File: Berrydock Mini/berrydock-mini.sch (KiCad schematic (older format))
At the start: 94 parts, among them J1 RJ45, P1 CONN_01X16, P2 CONN_01X11, P3 CONN_01X04, P4 CONN_01X03, P5 USB_OTG, P6 USB_A, SW1 SWITCH_INV, SW2 BUTTON, U1 USBLC6-2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

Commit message: laid everything out
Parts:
- removed C2, C3: 100nF, Capacitors_SMD:C_0603, symbol C_Small
- removed JP1, JP2: Jumper_NO_Small, Pin_Headers:Pin_Header_Straight_1x02, symbol Jumper_NO_Small
- removed R2: 2K, Resistors_SMD:R_0603_HandSoldering, symbol R_Small
- removed R3: 3K, Resistors_SMD:R_0603_HandSoldering, symbol R_Small
- removed U1, U2: USBLC6-2, Omega2-Berrydock:SOT32-6L, symbol USBLC6-2
- removed U6, U7: SMP75, Omega2-Berrydock:DO-214AA, symbol SMP75
- R11, R12, R6, R7, R8, R9: footprint Resistors_SMD:R_0603_HandSoldering -> Resistors_SMD:R_0603
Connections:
- net labels removed: CHARGE
- wire segments 368 -> 326
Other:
- note removed: "Power Sensing"

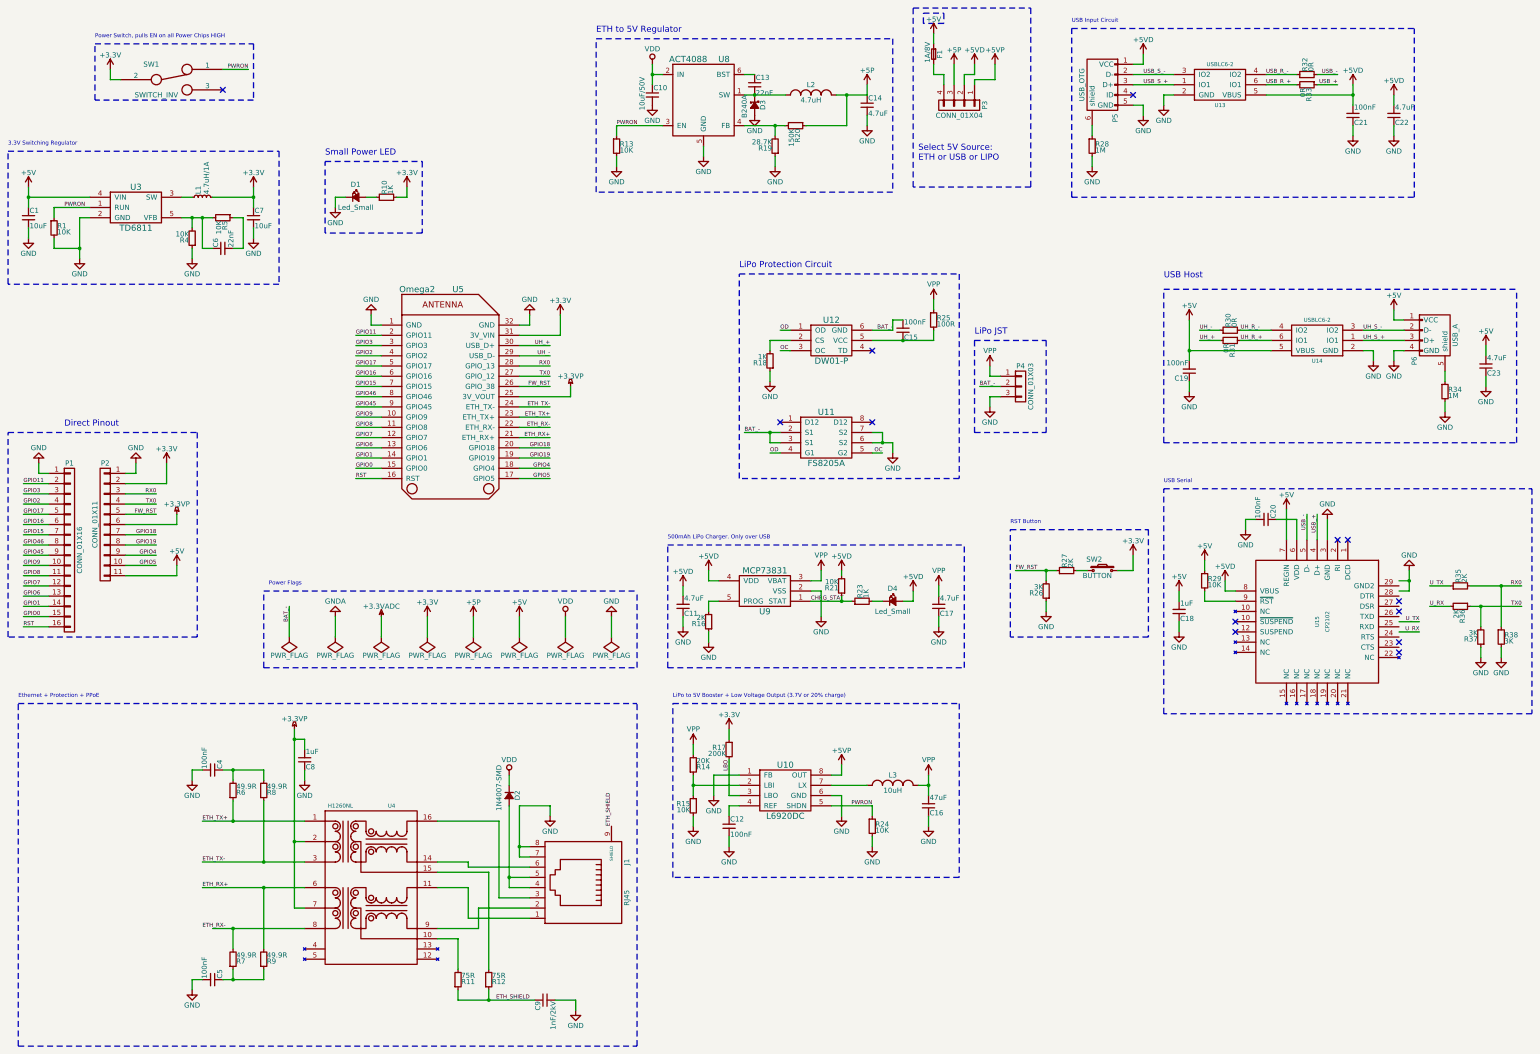
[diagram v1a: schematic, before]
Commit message: Finished Routing, only BoM and some nice graphics left to do
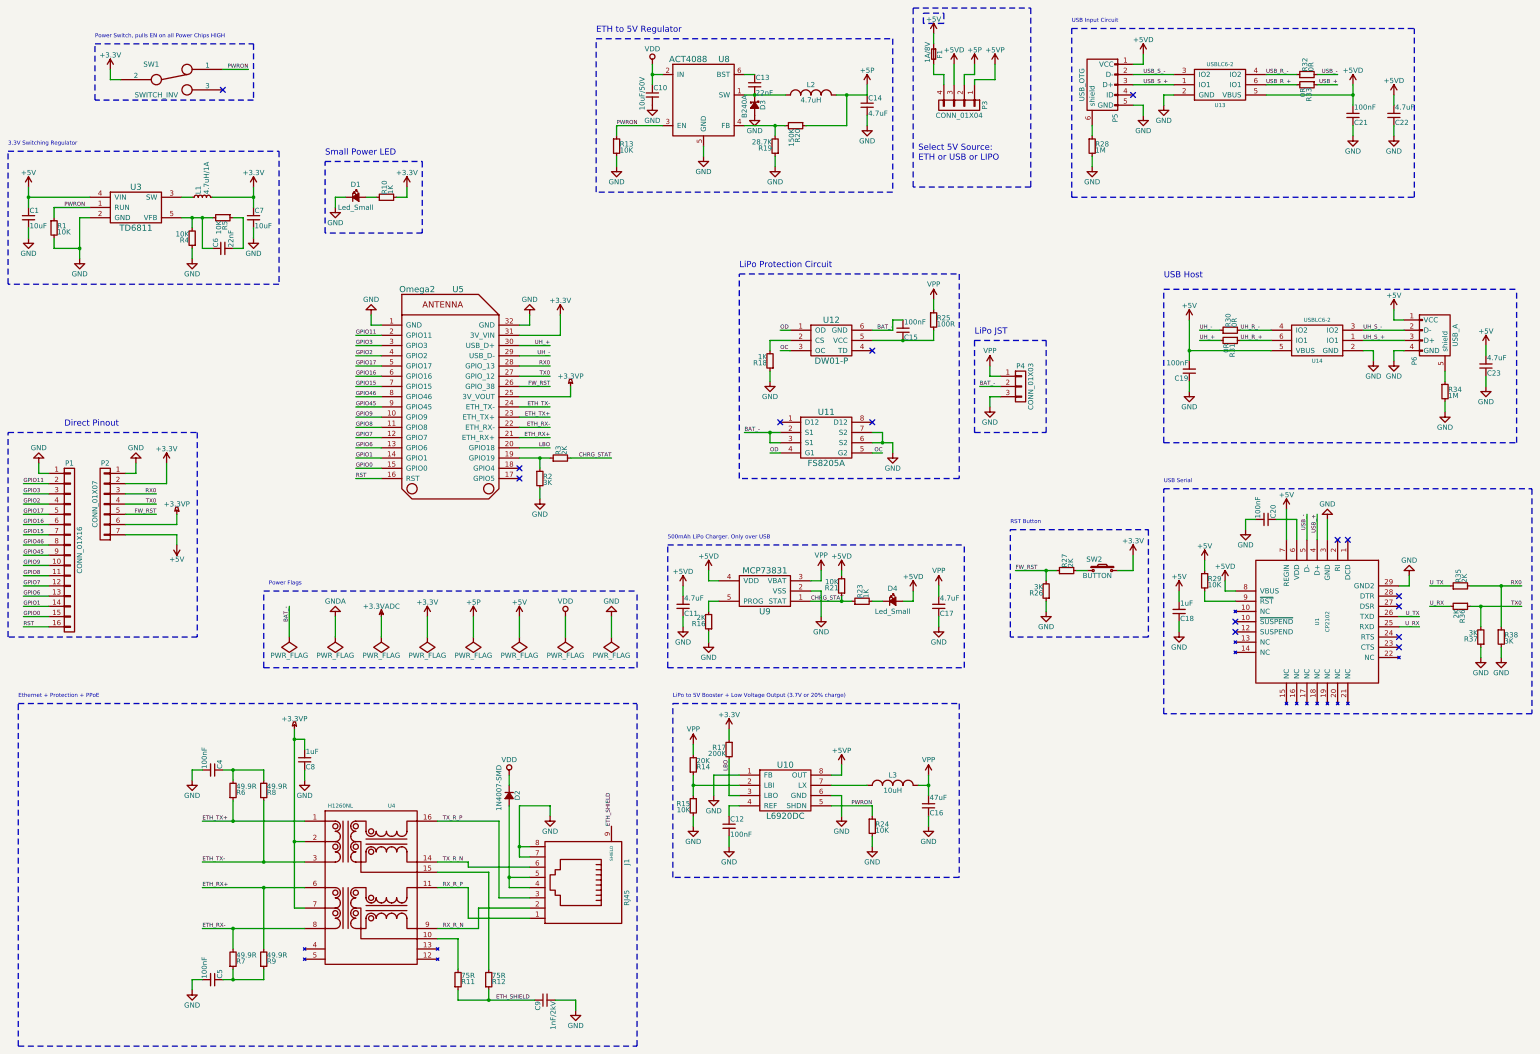
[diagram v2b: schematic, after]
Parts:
- removed P2: CONN_01X11, Pin_Headers:Pin_Header_Straight_1x11, symbol CONN_01X11
- removed U15: CP2102, Housings_DFN_QFN:QFN-28-1EP_5x5mm_Pitch0.5mm, symbol CP2102
- added P2: CONN_01X07, Pin_Headers:Pin_Header_Straight_1x07, symbol CONN_01X07
- added R2: 3K, Resistors_SMD:R_0603, symbol R_Small
- added R3: 2K, Resistors_SMD:R_0603, symbol R_Small
- added U1: CP2102, Omega2-Berrydock:QFN-28, symbol CP2102
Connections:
- net GPIO18 is gone; now on net LBO: U5.20 (GPIO18)
- net +3.3VP: now also P2.6 (P6)
- net +3V3: now also P2.2 (P2)
- net +5P: now also P3.2 (P2); no longer P3.3 (P3)
- net +5V: now also P2.7 (P7), U1.7 (REGIN)
- net +5VD: now also P3.3 (P3), U1.8 (VBUS); no longer P3.2 (P2)
- net CHRG_STAT: now also R3.2
- net ETH_RX-: now also R7.2, U4.8
- net FW_RST: now also P2.5 (P5)
- net GND: now also P2.1 (P1), R2.2, U1.29 (GND2), U1.3 (GND)
- net RX0: now also P2.3 (P3)
- net TX0: now also P2.4 (P4)
- net USB_+: now also U1.4 (D+)
- net USB_-: now also U1.5 (D-)
- net U_RX: now also U1.25 (RXD)
- net U_TX: now also U1.26 (TXD)
- net RX_R_P: now reaches J1.1, U4.11
- net RX_R_N: now reaches J1.2, U4.9
- net TX_R_P: now reaches J1.3, U4.16
- net TX_R_N: now reaches J1.6, U4.14
- net at C20.1: now also U1.6 (VDD)
- net at R29.2: now also U1.9 (~RST)
- net GPIO19: no longer names the net of U5.19 (GPIO19)
- net GPIO19: now also R2.1, R3.1
- net GPIO4: no longer names the net of U5.18 (GPIO4)
- net GPIO5: no longer names the net of U5.17 (GPIO5)
- no-connect marks 13 -> 15
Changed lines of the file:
@@
 EESchema Schematic File Version 2
+LIBS:berrydock-mini-rescue
 LIBS:power
 LIBS:device
@@
 L +5P #PWR010
 U 1 1 57E865D7
-P 10000 1350
-F 0 "#PWR010" H 10000 1200 50  0001 C CNN
-F 1 "+5P" H 10000 1490 50  0000 C CNN
-F 2 "" H 10000 1350 50  0000 C CNN
-F 3 "" H 10000 1350 50  0000 C CNN
-	1    10000 1350
+P 10200 1350
+F 0 "#PWR010" H 10200 1200 50  0001 C CNN
+F 1 "+5P" H 10200 1490 50  0000 C CNN
+F 2 "" H 10200 1350 50  0000 C CNN
+F 3 "" H 10200 1350 50  0000 C CNN
+	1    10200 1350
 	1    0    0    -1
 $EndComp
@@
 L +5VD #PWR011
 U 1 1 57E86633
-P 10200 1350
-F 0 "#PWR011" H 10200 1200 50  0001 C CNN
-F 1 "+5VD" H 10200 1490 50  0000 C CNN
-F 2 "" H 10200 1350 50  0000 C CNN
-F 3 "" H 10200 1350 50  0000 C CNN
-	1    10200 1350
+P 10000 1350
+F 0 "#PWR011" H 10000 1200 50  0001 C CNN
+F 1 "+5VD" H 10000 1490 50  0000 C CNN
+F 2 "" H 10000 1350 50  0000 C CNN
+F 3 "" H 10000 1350 50  0000 C CNN
+	1    10000 1350
 	1    0    0    -1
 $EndComp
@@
 Text Label 6050 4500 2    39   ~ 0
 FW_RST
-Text Label 6050 5100 2    39   ~ 0
-GPIO18
-Text Label 6050 5200 2    39   ~ 0
-GPIO19
-Text Label 6050 5300 2    39   ~ 0
-GPIO4
-Text Label 6050 5400 2    39   ~ 0
-GPIO5
 Text Label 10600 6300 0    39   ~ 0
 FW_RST
@@
 Text Label 2200 5750 2    39   ~ 0
 FW_RST
-Text Label 2200 5950 2    39   ~ 0
-GPIO18
-Text Label 2200 6050 2    39   ~ 0
-GPIO19
-Text Label 2200 6150 2    39   ~ 0
-GPIO4
-Text Label 2200 6250 2    39   ~ 0
-GPIO5
 $Comp
 L GND #PWR065
@@
 L GND #PWR068
 U 1 1 57EB7E96
-P 14450 6300
-F 0 "#PWR068" H 14450 6050 50  0001 C CNN
-F 1 "GND" H 14450 6150 50  0000 C CNN
-F 2 "" H 14450 6300 50  0000 C CNN
-F 3 "" H 14450 6300 50  0000 C CNN
-	1    14450 6300
+P 14450 6350
+F 0 "#PWR068" H 14450 6100 50  0001 C CNN
+F 1 "GND" H 14450 6200 50  0000 C CNN
+F 2 "" H 14450 6350 50  0000 C CNN
+F 3 "" H 14450 6350 50  0000 C CNN
+	1    14450 6350
 	-1   0    0    1
 $EndComp
@@
 Text Label 15550 6650 2    39   ~ 0
 TX0
-NoConn ~ 14350 6600
-NoConn ~ 14350 6700
-NoConn ~ 14350 7000
-NoConn ~ 14350 7100
 NoConn ~ 12750 6900
 NoConn ~ 12750 6800
@@
 	1    0    0    -1
 $EndComp
-Text Label 14550 6800 2    39   ~ 0
+Text Label 14550 6750 2    39   ~ 0
 U_TX
-Text Label 14550 6900 2    39   ~ 0
+Text Label 14550 6850 2    39   ~ 0
 U_RX
 $Comp
@@
 $EndComp
 $Comp
-L CP2102 U15
-U 1 1 57E98E28
-P 13550 6800
-F 0 "U15" H 13550 6800 39  0000 C CNN
-F 1 "CP2102" H 13550 6900 39  0000 C CNN
-F 2 "Housings_DFN_QFN:QFN-28-1EP_5x5mm_Pitch0.5mm" H 13550 6800 39  0001 C CNN
-F 3 "" H 13550 6800 39  0001 C CNN
-	1    13550 6800
-	0    1    1    0
-$EndComp
-$Comp
 L R_Small R29
 U 1 1 57E9C495
@@
 L +5V #PWR0104
 U 1 1 57EC78AB
-P 2400 6250
-F 0 "#PWR0104" H 2400 6100 50  0001 C CNN
-F 1 "+5V" H 2400 6390 50  0000 C CNN
-F 2 "" H 2400 6250 50  0000 C CNN
-F 3 "" H 2400 6250 50  0000 C CNN
-	1    2400 6250
-	1    0    0    -1
-$EndComp
-$Comp
-L CONN_01X11 P2
-U 1 1 57EC8677
-P 1700 5850
-F 0 "P2" H 1700 6450 50  0000 C CNN
-F 1 "CONN_01X11" V 1800 5850 50  0000 C CNN
-F 2 "Pin_Headers:Pin_Header_Straight_1x11" H 1700 5850 50  0001 C CNN
-F 3 "" H 1700 5850 50  0000 C CNN
-	1    1700 5850
-	-1   0    0    -1
+P 2400 6050
+F 0 "#PWR0104" H 2400 5900 50  0001 C CNN
+F 1 "+5V" H 2400 6190 50  0000 C CNN
+F 2 "" H 2400 6050 50  0000 C CNN
+F 3 "" H 2400 6050 50  0000 C CNN
+	1    2400 6050
+	1    0    0    1
 $EndComp
 $Comp
@@
 	2650 9400 3650 9400
 Wire Wire Line
-	2750 9800 3650 9800
+	2650 9800 3650 9800
 Wire Wire Line
 	3250 10000 3250 9400
@@
 Wire Wire Line
 	1150 6750 900  6750
-Wire Wire Line
-	2200 5950 1900 5950
-Wire Wire Line
-	1900 6050 2200 6050
-Wire Wire Line
-	2200 6150 1900 6150
-Wire Wire Line
-	1900 6250 2200 6250
-Wire Wire Line
-	6050 5400 5750 5400
-Wire Wire Line
-	5750 5300 6050 5300
-Wire Wire Line
-	6050 5200 5750 5200
-Wire Wire Line
-	5750 5100 6050 5100
 Wire Notes Line
 	750  4950 2600 4950
@@
 	13650 5800 13650 6000
 Wire Wire Line
-	14450 6500 14350 6500
-Wire Wire Line
-	14450 6300 14450 6500
-Wire Wire Line
-	14350 6400 14450 6400
-Connection ~ 14450 6400
+	14350 6450 14450 6450
 Wire Wire Line
 	12750 6600 12450 6600
 Wire Wire Line
-	14550 6900 14350 6900
+	14550 6850 14350 6850
 Wire Wire Line
-	14350 6800 14550 6800
+	14350 6750 14550 6750
 Wire Wire Line
 	14650 6650 14850 6650
@@
 	750  6950 750  4950
 Wire Wire Line
-	2400 6250 2400 6350
+	2400 6050 2400 5950
 Wire Wire Line
-	2400 6350 1900 6350
+	2400 5950 1900 5950
+Text Label 5000 8750 0    39   ~ 0
+TX_R_P
+Text Label 5000 9150 0    39   ~ 0
+TX_R_N
+Text Label 5000 9400 0    39   ~ 0
+RX_R_P
+Text Label 5000 9800 0    39   ~ 0
+RX_R_N
+$Comp
+L CONN_01X07 P2
+U 1 1 57ED44BA
+P 1700 5650
+F 0 "P2" H 1700 6050 50  0000 C CNN
+F 1 "CONN_01X07" V 1800 5650 50  0000 C CNN
+F 2 "Pin_Headers:Pin_Header_Straight_1x07" H 1700 5650 50  0001 C CNN
+F 3 "" H 1700 5650 50  0000 C CNN
+	1    1700 5650
+	-1   0    0    -1
+$EndComp
+NoConn ~ 5750 5300
+NoConn ~ 5750 5400
+Text Label 6050 5100 2    39   ~ 0
+LBO
+Wire Wire Line
+	6050 5100 5750 5100
+Text Label 6650 5200 2    39   ~ 0
+CHRG_STAT
+$Comp
+L R_Small R3
+U 1 1 57ED7E01
+P 6150 5200
+F 0 "R3" H 6180 5220 50  0000 L CNN
+F 1 "2K" H 6180 5160 50  0000 L CNN
+F 2 "Resistors_SMD:R_0603" H 6150 5200 50  0001 C CNN
+F 3 "" H 6150 5200 50  0000 C CNN
+	1    6150 5200
+	0    -1   -1   0
+$EndComp
+$Comp
+L R_Small R2
+U 1 1 57ED7F30
+P 5950 5400
+F 0 "R2" H 5980 5420 50  0000 L CNN
+F 1 "3K" H 5980 5360 50  0000 L CNN
+F 2 "Resistors_SMD:R_0603" H 5950 5400 50  0001 C CNN
+F 3 "" H 5950 5400 50  0000 C CNN
+	1    5950 5400
+	1    0    0    -1
+$EndComp
+Wire Wire Line
+	5750 5200 6050 5200
+Wire Wire Line
+	6650 5200 6250 5200
+Wire Wire Line
+	5950 5300 5950 5200
+Connection ~ 5950 5200
+$Comp
+L GND #PWR0106
+U 1 1 57EDA23D
+P 5950 5600
+F 0 "#PWR0106" H 5950 5350 50  0001 C CNN
+F 1 "GND" H 5950 5450 50  0000 C CNN
+F 2 "" H 5950 5600 50  0000 C CNN
+F 3 "" H 5950 5600 50  0000 C CNN
+	1    5950 5600
+	1    0    0    -1
+$EndComp
+Wire Wire Line
+	5950 5600 5950 5500
+Wire Wire Line
+	14450 6450 14450 6350
+$Comp
+L CP2102 U1
+U 1 1 57ED4EEB
+P 13550 6800
+F 0 "U1" H 13550 6800 39  0000 C CNN
+F 1 "CP2102" H 13550 6900 39  0000 C CNN
+F 2 "Omega2-Berrydock:QFN-28" H 13550 6800 39  0001 C CNN
+F 3 "" H 13550 6800 39  0001 C CNN
+	1    13550 6800
+	0    1    1    0
+$EndComp
+NoConn ~ 14350 7050
+NoConn ~ 14350 6950
+NoConn ~ 14350 6650
+NoConn ~ 14350 6550
 $EndSCHEMATC

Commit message: Finished BOM Cost
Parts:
- C6: footprint Capacitors_SMD:C_1206 -> Capacitors_SMD:C_0603
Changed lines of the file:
@@
 F 0 "C6" H 2860 3220 50  0000 L CNN
 F 1 "22nF" H 2860 3070 50  0000 L CNN
-F 2 "Capacitors_SMD:C_1206" H 2850 3150 50  0001 C CNN
+F 2 "Capacitors_SMD:C_0603" H 2850 3150 50  0001 C CNN
 F 3 "" H 2850 3150 50  0000 C CNN
 	1    2850 3150

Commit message: changed all resistor footprints to 0603, added CE8301A50P component
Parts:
- R1, R10, R13, R14, R15, R16, R17, R19, R20, R21, R23, R24, R26, R27, R28, R29, R32, R33, R35, R36, R37, R38, R4, R5: footprint Resistors_SMD:R_0603_HandSoldering -> Resistors_SMD:R_0603
- U8: footprint TO_SOT_Packages_SMD:SOT-23-6_Handsoldering -> TO_SOT_Packages_SMD:SOT-23-6
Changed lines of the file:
@@
 F 0 "U8" H 7750 2100 60  0000 C CNN
 F 1 "ACT4088" H 7400 2100 60  0000 C CNN
-F 2 "TO_SOT_Packages_SMD:SOT-23-6_Handsoldering" H 7650 1650 60  0001 C CNN
+F 2 "TO_SOT_Packages_SMD:SOT-23-6" H 7650 1650 60  0001 C CNN
 F 3 "" H 7650 1650 60  0001 C CNN
 	1    7550 1700
@@
 F 0 "R13" H 6730 2170 50  0000 L CNN
 F 1 "10K" H 6730 2110 50  0000 L CNN
-F 2 "Resistors_SMD:R_0603_HandSoldering" H 6700 2150 50  0001 C CNN
+F 2 "Resistors_SMD:R_0603" H 6700 2150 50  0001 C CNN
 F 3 "" H 6700 2150 50  0000 C CNN
 	1    6700 2150
@@
 F 0 "R20" H 8480 1970 50  0000 L CNN
 F 1 "150K" H 8480 1910 50  0000 L CNN
-F 2 "Resistors_SMD:R_0603_HandSoldering" H 8450 1950 50  0001 C CNN
+F 2 "Resistors_SMD:R_0603" H 8450 1950 50  0001 C CNN
 F 3 "" H 8450 1950 50  0000 C CNN
 	1    8450 1950
@@
 F 0 "R19" H 8280 2170 50  0000 L CNN
 F 1 "28.7K" H 8280 2110 50  0000 L CNN
-F 2 "Resistors_SMD:R_0603_HandSoldering" H 8250 2150 50  0001 C CNN
+F 2 "Resistors_SMD:R_0603" H 8250 2150 50  0001 C CNN
 F 3 "" H 8250 2150 50  0000 C CNN
 	1    8250 2150
@@
 F 0 "R16" H 7630 6820 50  0000 L CNN
 F 1 "2K" H 7630 6760 50  0000 L CNN
-F 2 "Resistors_SMD:R_0603_HandSoldering" H 7600 6800 50  0001 C CNN
+F 2 "Resistors_SMD:R_0603" H 7600 6800 50  0001 C CNN
 F 3 "" H 7600 6800 50  0000 C CNN
 	1    7600 6800
@@
 F 0 "R14" H 7480 8220 50  0000 L CNN
 F 1 "20K" H 7480 8160 50  0000 L CNN
-F 2 "Resistors_SMD:R_0603_HandSoldering" H 7450 8200 50  0001 C CNN
+F 2 "Resistors_SMD:R_0603" H 7450 8200 50  0001 C CNN
 F 3 "" H 7450 8200 50  0000 C CNN
 	1    7450 8200
@@
 F 0 "R15" H 7480 8620 50  0000 L CNN
 F 1 "10K" H 7480 8560 50  0000 L CNN
-F 2 "Resistors_SMD:R_0603_HandSoldering" H 7450 8600 50  0001 C CNN
+F 2 "Resistors_SMD:R_0603" H 7450 8600 50  0001 C CNN
 F 3 "" H 7450 8600 50  0000 C CNN
 	1    7450 8600
@@
 F 0 "R17" H 7830 8070 50  0000 L CNN
 F 1 "200K" H 7830 8010 50  0000 L CNN
-F 2 "Resistors_SMD:R_0603_HandSoldering" H 7800 8050 50  0001 C CNN
+F 2 "Resistors_SMD:R_0603" H 7800 8050 50  0001 C CNN
 F 3 "" H 7800 8050 50  0000 C CNN
 	1    7800 8050
@@
 F 0 "R28" H 11380 2170 50  0000 L CNN
 F 1 "1M" H 11380 2110 50  0000 L CNN
-F 2 "Resistors_SMD:R_0603_HandSoldering" H 11350 2150 50  0001 C CNN
+F 2 "Resistors_SMD:R_0603" H 11350 2150 50  0001 C CNN
 F 3 "" H 11350 2150 50  0000 C CNN
 	1    11350 2150
@@
 F 0 "R27" H 11130 6320 50  0000 L CNN
 F 1 "2K" H 11130 6260 50  0000 L CNN
-F 2 "Resistors_SMD:R_0603_HandSoldering" H 11100 6300 50  0001 C CNN
+F 2 "Resistors_SMD:R_0603" H 11100 6300 50  0001 C CNN
 F 3 "" H 11100 6300 50  0000 C CNN
 	1    11100 6300
@@
 F 0 "R26" H 10930 6520 50  0000 L CNN
 F 1 "3K" H 10930 6460 50  0000 L CNN
-F 2 "Resistors_SMD:R_0603_HandSoldering" H 10900 6500 50  0001 C CNN
+F 2 "Resistors_SMD:R_0603" H 10900 6500 50  0001 C CNN
 F 3 "" H 10900 6500 50  0000 C CNN
 	1    10900 6500
@@
 F 0 "R32" H 13480 1470 50  0000 L CNN
 F 1 "0R" H 13480 1410 50  0000 L CNN
-F 2 "Resistors_SMD:R_0603_HandSoldering" H 13450 1450 50  0001 C CNN
+F 2 "Resistors_SMD:R_0603" H 13450 1450 50  0001 C CNN
 F 3 "" H 13450 1450 50  0000 C CNN
 	1    13450 1450
@@
 F 0 "R33" H 13480 1570 50  0000 L CNN
 F 1 "0R" H 13480 1510 50  0000 L CNN
-F 2 "Resistors_SMD:R_0603_HandSoldering" H 13450 1550 50  0001 C CNN
+F 2 "Resistors_SMD:R_0603" H 13450 1550 50  0001 C CNN
 F 3 "" H 13450 1550 50  0000 C CNN
 	1    13450 1550
@@
 F 0 "R37" H 15180 6970 50  0000 L CNN
 F 1 "3K" H 15180 6910 50  0000 L CNN
-F 2 "Resistors_SMD:R_0603_HandSoldering" H 15150 6950 50  0001 C CNN
+F 2 "Resistors_SMD:R_0603" H 15150 6950 50  0001 C CNN
 F 3 "" H 15150 6950 50  0000 C CNN
 	1    15150 6950
@@
 F 0 "R38" H 15380 6970 50  0000 L CNN
 F 1 "3K" H 15380 6910 50  0000 L CNN
-F 2 "Resistors_SMD:R_0603_HandSoldering" H 15350 6950 50  0001 C CNN
+F 2 "Resistors_SMD:R_0603" H 15350 6950 50  0001 C CNN
 F 3 "" H 15350 6950 50  0000 C CNN
 	1    15350 6950
@@
 F 0 "R36" H 14980 6670 50  0000 L CNN
 F 1 "2K" H 14980 6610 50  0000 L CNN
-F 2 "Resistors_SMD:R_0603_HandSoldering" H 14950 6650 50  0001 C CNN
+F 2 "Resistors_SMD:R_0603" H 14950 6650 50  0001 C CNN
 F 3 "" H 14950 6650 50  0000 C CNN
 	1    14950 6650
@@
 F 0 "R35" H 14980 6470 50  0000 L CNN
 F 1 "2K" H 14980 6410 50  0000 L CNN
-F 2 "Resistors_SMD:R_0603_HandSoldering" H 14950 6450 50  0001 C CNN
+F 2 "Resistors_SMD:R_0603" H 14950 6450 50  0001 C CNN
 F 3 "" H 14950 6450 50  0000 C CNN
 	1    14950 6450
@@
 F 0 "R29" H 12480 6420 50  0000 L CNN
 F 1 "10K" H 12480 6360 50  0000 L CNN
-F 2 "Resistors_SMD:R_0603_HandSoldering" H 12450 6400 50  0001 C CNN
+F 2 "Resistors_SMD:R_0603" H 12450 6400 50  0001 C CNN
 F 3 "" H 12450 6400 50  0000 C CNN
 	1    12450 6400
@@
 F 0 "R21" H 8930 6470 50  0000 L CNN
 F 1 "10K" H 8930 6410 50  0000 L CNN
-F 2 "Resistors_SMD:R_0603_HandSoldering" H 8900 6450 50  0001 C CNN
+F 2 "Resistors_SMD:R_0603" H 8900 6450 50  0001 C CNN
 F 3 "" H 8900 6450 50  0000 C CNN
 	1    8900 6450
@@
 F 0 "R1" H 1230 2970 50  0000 L CNN
 F 1 "10K" H 1230 2910 50  0000 L CNN
-F 2 "Resistors_SMD:R_0603_HandSoldering" H 1200 2950 50  0001 C CNN
+F 2 "Resistors_SMD:R_0603" H 1200 2950 50  0001 C CNN
 F 3 "" H 1200 2950 50  0000 C CNN
 	1    1200 2950
@@
 F 0 "R5" H 2880 2870 50  0000 L CNN
 F 1 "10K" H 2880 2810 50  0000 L CNN
-F 2 "Resistors_SMD:R_0603_HandSoldering" H 2850 2850 50  0001 C CNN
+F 2 "Resistors_SMD:R_0603" H 2850 2850 50  0001 C CNN
 F 3 "" H 2850 2850 50  0000 C CNN
 	1    2850 2850
@@
 F 0 "R4" H 2580 3070 50  0000 L CNN
 F 1 "10K" H 2580 3010 50  0000 L CNN
-F 2 "Resistors_SMD:R_0603_HandSoldering" H 2550 3050 50  0001 C CNN
+F 2 "Resistors_SMD:R_0603" H 2550 3050 50  0001 C CNN
 F 3 "" H 2550 3050 50  0000 C CNN
 	1    2550 3050
@@
 F 0 "R24" H 9230 8820 50  0000 L CNN
 F 1 "10K" H 9230 8760 50  0000 L CNN
-F 2 "Resistors_SMD:R_0603_HandSoldering" H 9200 8800 50  0001 C CNN
+F 2 "Resistors_SMD:R_0603" H 9200 8800 50  0001 C CNN
 F 3 "" H 9200 8800 50  0000 C CNN
 	1    9200 8800
@@
 F 0 "R23" H 9130 6620 50  0000 L CNN
 F 1 "1K" H 9130 6560 50  0000 L CNN
-F 2 "Resistors_SMD:R_0603_HandSoldering" H 9100 6600 50  0001 C CNN
+F 2 "Resistors_SMD:R_0603" H 9100 6600 50  0001 C CNN
 F 3 "" H 9100 6600 50  0000 C CNN
 	1    9100 6600
@@
 F 0 "R10" H 4480 2670 50  0000 L CNN
 F 1 "1K" H 4480 2610 50  0000 L CNN
-F 2 "Resistors_SMD:R_0603_HandSoldering" H 4450 2650 50  0001 C CNN
+F 2 "Resistors_SMD:R_0603" H 4450 2650 50  0001 C CNN
 F 3 "" H 4450 2650 50  0000 C CNN
 	1    4450 2650
